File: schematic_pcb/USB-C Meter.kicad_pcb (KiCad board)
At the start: 2 copper layers, 49.4 x 45 mm, 57 parts, among them J1 USB_B_Micro, J2 USB-C Receptacle 6P, J3 Generic IN, J4 Generic OUT, J5 USB-C Receptacle 6P, J6 Conn_Coaxial, J7 UART, U1 XL1509-3.3, U2 ME6211C33, U3 TPS2115, U4 ESP32-C3FH4, U6 INA228, U7 Display I2C, Y1 40MHz

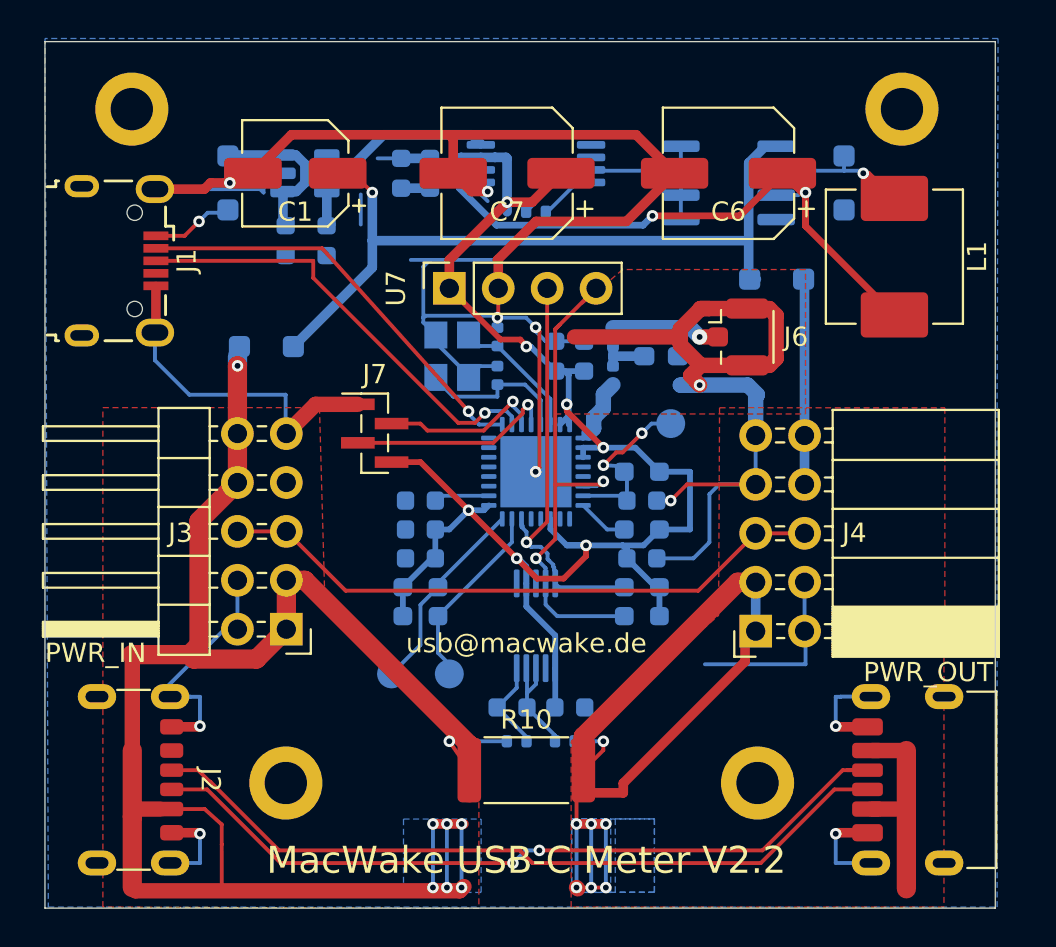
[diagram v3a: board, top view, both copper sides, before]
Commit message: feat(hw): new buck converter enables up to 48V PD input
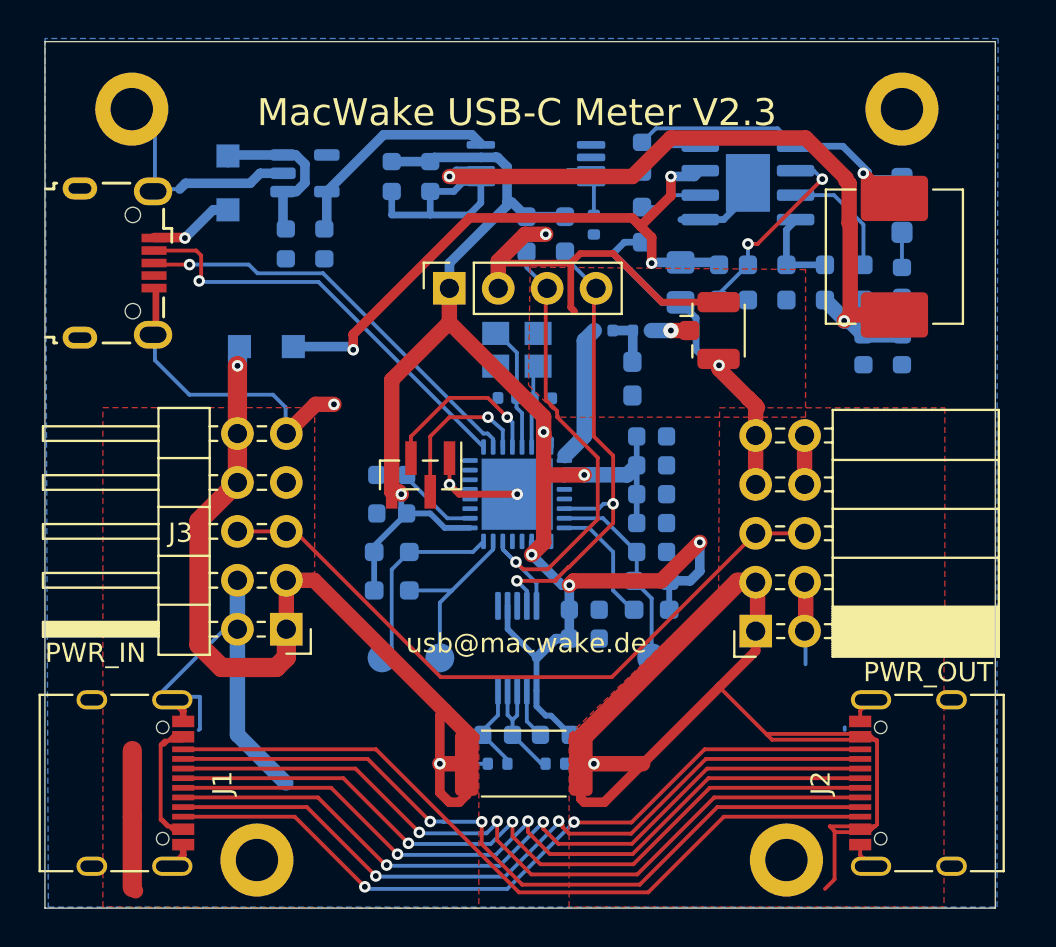
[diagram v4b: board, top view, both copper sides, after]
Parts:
- removed C2, C3: 10µF/10V, Capacitor_SMD:C_0603_1608Metric
- removed D4: 1N5819WS, Diode_SMD:D_SOD-123F
- removed U7: Display I2C, Connector_PinSocket_2.54mm:PinSocket_1x04_P2.54mm_Vertical
- added C19: 1µ, Capacitor_SMD:C_0603_1608Metric, B.Cu at (90.0, 47.7)
- added C22: 27pF, Capacitor_SMD:C_0402_1005Metric, B.Cu at (84.3, 44.2)
- added C23: 27pF, Capacitor_SMD:C_0402_1005Metric, B.Cu at (82.5, 44.2)
- added C24: 1pF, Capacitor_SMD:C_0402_1005Metric, B.Cu at (87.5, 40.7)
- added C25: 1pF, Capacitor_SMD:C_0402_1005Metric, B.Cu at (89.5, 40.7)
- added C26: 0.1µ, Capacitor_SMD:C_0603_1608Metric, B.Cu at (85.0, 61.7)
- added J8: UART, Connector_PinHeader_1.00mm:PinHeader_1x04_P1.00mm_Vertical_SMD_Pin1Left, F.Cu at (78.0, 48.2)
- added R15: 12k, Resistor_SMD:R_0603_1608Metric_Pad0.98x0.95mm_HandSolder, B.Cu at (76.5, 52.2)
- added R16: 12k, Resistor_SMD:R_0603_1608Metric_Pad0.98x0.95mm_HandSolder, B.Cu at (90.0, 53.7)
- added R5: 33k, Resistor_SMD:R_0603_1608Metric_Pad0.98x0.95mm_HandSolder, B.Cu at (95.0, 38.2)
- added R6: 200k, Resistor_SMD:R_0603_1608Metric_Pad0.98x0.95mm_HandSolder, B.Cu at (89.5, 35.2)
- added R7: 68k, Resistor_SMD:R_0603_1608Metric_Pad0.98x0.95mm_HandSolder, B.Cu at (99.0, 38.2)
- added R8: 22k, Resistor_SMD:R_0603_1608Metric_Pad0.98x0.95mm_HandSolder, B.Cu at (97.0, 38.2)
- C1: value 33µF/35V -> 0.1µ; footprint Capacitor_SMD:CP_Elec_5x5.8 -> Capacitor_SMD:C_0603_1608Metric; moved to B.Cu
- C10, C12: value 0.1µ -> 10µ
- C11: value 1µ -> 10µ
- C13: value 0.1µ -> 10µF
- C15: value 10n -> 0.1µ
- C17, C18: value 1pF -> 0.1µ; footprint Capacitor_SMD:C_0402_1005Metric -> Capacitor_SMD:C_0603_1608Metric
- C20: value 0.1µ -> 10n
- C21: value 0.1µF/6.3V -> 0.1µ
- C4: value 27pF -> 4.7µ; footprint Capacitor_SMD:C_0402_1005Metric -> Capacitor_SMD:C_0805_2012Metric_Pad1.18x1.45mm_HandSolder
- C5: value 27pF -> 10µ; footprint Capacitor_SMD:C_0402_1005Metric -> Capacitor_SMD:C_0603_1608Metric
- C6: value 220µF -> 10µ; footprint Capacitor_SMD:CP_Elec_6.3x5.9 -> Capacitor_SMD:C_0603_1608Metric; moved to B.Cu
- C7: value 220µF -> 0.1µ; footprint Capacitor_SMD:CP_Elec_6.3x5.9 -> Capacitor_SMD:C_0603_1608Metric; moved to B.Cu
- C8: value 0.1µ -> 2.2n
- C9: value 10µF -> 10µF/10V
- D1, D3: value 1N5819WS -> CMMSH1-60G; footprint Diode_SMD:D_SOD-123F -> Diode_SMD:Nexperia_CFP3_SOD-123W
- J1: value USB_B_Micro -> USB-C Receptacle 6P; footprint Connector_USB:USB_Micro-B_Wuerth_629105150521 -> Connector_USB:USB_C_Receptacle_XKB_U262-16XN-4BVC11
- J2: footprint Connector_USB:USB_C_Receptacle_GCT_USB4125-xx-x_6P_TopMnt_Horizontal -> Connector_USB:USB_C_Receptacle_XKB_U262-16XN-4BVC11
- J5: value USB-C Receptacle 6P -> USB_B_Micro; footprint Connector_USB:USB_C_Receptacle_HRO_TYPE-C-31-M-17 -> Connector_USB:USB_Micro-B_Wuerth_629105150521
- J6: value Conn_Coaxial -> Display I2C; footprint Connector_Coaxial:U.FL_Hirose_U.FL-R-SMT-1_Vertical -> Connector_PinSocket_2.54mm:PinSocket_1x04_P2.54mm_Vertical
- J7: value UART -> Conn_Coaxial; footprint Connector_PinHeader_1.00mm:PinHeader_1x04_P1.00mm_Vertical_SMD_Pin1Left -> Connector_Coaxial:U.FL_Hirose_U.FL-R-SMT-1_Vertical
- R1: value 3k3 -> 0.01R 3W; footprint Resistor_SMD:R_0603_1608Metric_Pad0.98x0.95mm_HandSolder -> Resistor_SMD:R_2512_6332Metric; moved to F.Cu
- R10: value 0.01R 3W -> 400R; footprint Resistor_SMD:R_2512_6332Metric -> Resistor_SMD:R_0402_1005Metric; moved to B.Cu
- R11: value 10R -> 3k3; footprint Resistor_SMD:R_0402_1005Metric -> Resistor_SMD:R_0603_1608Metric_Pad0.98x0.95mm_HandSolder
- R12: value 12k -> 3k3
- R2: value 3k3 -> 10R; footprint Resistor_SMD:R_0603_1608Metric_Pad0.98x0.95mm_HandSolder -> Resistor_SMD:R_0402_1005Metric
- R3: value 400R -> 10R
- R4: value 12k -> 100k
- R9: value 10R -> 56k; footprint Resistor_SMD:R_0402_1005Metric -> Resistor_SMD:R_0603_1608Metric_Pad0.98x0.95mm_HandSolder
- TP2: value Expansion -> Exp
- U1: value XL1509-3.3 -> MP4560DN; footprint Package_SO:SOIC-8_3.9x4.9mm_P1.27mm -> Package_SO:SOIC-8-1EP_3.9x4.9mm_P1.27mm_EP2.29x3mm
- moved J5 50.0 mm to (62.3, 37.2), turned to -90 degrees
- moved J2 42.5 mm to (104.5, 64.2), turned to 90 degrees
- moved C1 31.0 mm to (82.0, 61.7), turned to 0 degrees
- moved R9 29.9 mm to (101.0, 38.2), turned to 90 degrees
- moved R3 28.7 mm to (85.0, 63.2), turned to 0 degrees
- moved R10 28.5 mm to (87.0, 35.2), turned to -90 degrees
- moved J1 27.1 mm to (62.0, 64.2)
- moved C8 26.6 mm to (103.0, 38.2)
- moved R11 26.3 mm to (85.5, 35.7), turned to 90 degrees
- moved C10 23.2 mm to (73.0, 36.2), turned to -90 degrees
- moved C11 19.8 mm to (78.5, 32.7), turned to -90 degrees
- moved C5 19.0 mm to (101.0, 41.7)
- moved C12 18.4 mm to (76.5, 32.7), turned to -90 degrees
- moved J7 18.2 mm to (93.0, 40.7)
- moved R12 16.5 mm to (83.5, 35.7), turned to 90 degrees
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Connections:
- C1 pad 1: /VBUS_PD_R -> /SHNT+
- C1 pad 2: GND -> Net-(U6-Vbus)
- C10 pad 1: GND -> /VBUS_DATA_3V3
- C10 pad 2: 3V3 -> GND
- C12 pad 1: GND -> 3V3
- C12 pad 2: 3V3 -> GND
- C13 pad 1: GND -> 3V3
- C13 pad 2: Net-(U4-VDD_SPI) -> GND
- C14 pad 1: GND -> 3V3
- C14 pad 2: 3V3 -> GND
- C15 pad 1: GND -> 3V3
- C15 pad 2: 3V3 -> GND
- C16 pad 2: Net-(U4-CHIP_EN) -> 3V3
- C17 pad 1: /RF -> GND
- C17 pad 2: Net-(C17-Pad2) -> 3V3
- C18 pad 1: /ANT -> GND
- C18 pad 2: Net-(C17-Pad2) -> Net-(U4-VDD_SPI)
- C20 pad 1: 3V3 -> GND
- C20 pad 2: GND -> 3V3
- C21 pad 1: /SHNT+ -> GND
- C21 pad 2: /SHNT- -> Net-(U4-CHIP_EN)
- C4 pad 1: Net-(U4-XTAL_N) -> /VBUS_PD_R
- C5 pad 1: GND -> /VBUS_PD_3V3
- C5 pad 2: Net-(U4-XTAL_P) -> GND
- C7 pad 1: 3V3 -> Net-(U1-BST)
- C7 pad 2: GND -> Net-(D2-K)
- C8 pad 1: 3V3 -> Net-(C8-Pad1)
- C9 pad 1: 3V3 -> /VBUS_DATA_R
- J2 pad A9: /VBUS_PD_1_IN -> /VBUS_PD_2_IN
- J2 pad B9: /VBUS_PD_1_IN -> /VBUS_PD_2_IN
- J6 pad 1: /ANT -> 3V3
- J7 pad 1: GND -> /ANT
- J7 pad 2: Net-(J7-Pin_2) -> GND
- L2 pad 2: Net-(C17-Pad2) -> Net-(C24-Pad2)
- R1 pad 1: SDA -> /VBUS_PD_1_IN
- R1 pad 2: 3V3 -> /VBUS_PD_2_IN
- R10 pad 1: /VBUS_PD_1_IN -> Net-(U3-ILIM)
- R10 pad 2: /VBUS_PD_2_IN -> GND
- R11 pad 1: /SHNT- -> SDA
- R11 pad 2: /VBUS_PD_2_IN -> 3V3
- R12 pad 1: Net-(U4-GPIO3) -> SCL
- R13 pad 1: Net-(U4-GPIO9) -> Net-(U4-GPIO3)
- R14 pad 1: Net-(U4-GPIO10) -> Net-(U4-GPIO9)
- R2 pad 1: SCL -> /VBUS_PD_1_IN
- R2 pad 2: 3V3 -> /SHNT+
- R3 pad 1: Net-(U3-ILIM) -> Net-(U6-Vbus)
- R3 pad 2: GND -> /VBUS_PD_2_IN
- R4 pad 1: Net-(U4-CHIP_EN) -> Net-(U1-EN)
- R4 pad 2: 3V3 -> /VBUS_PD_R
- R9 pad 1: /SHNT+ -> Net-(C8-Pad1)
- R9 pad 2: /VBUS_PD_1_IN -> Net-(U1-COMP)
- U1 pad 1: /VBUS_PD_R -> Net-(D2-K)
- U1 pad 2: Net-(D2-K) -> Net-(U1-EN)
- U1 pad 3: /VBUS_PD_3V3 -> Net-(U1-COMP)
- U1 pad 4: GND -> Net-(U1-FB)
- U1 pad 6: GND -> Net-(U1-FREQ)
- U1 pad 7: GND -> /VBUS_PD_R
- U1 pad 8: GND -> Net-(U1-BST)
- U4 pad 25: Net-(J1-D-) -> /D-
- U4 pad 26: Net-(J1-D+) -> /D+
- U4 pad 27: Net-(J7-Pin_2) -> Net-(J8-Pin_2)
- U4 pad 28: Net-(J7-Pin_3) -> Net-(J8-Pin_3)
- U6 pad 8: /SHNT- -> Net-(U6-Vbus)
- U6 pad 9: /SHNT- -> Net-(U6-Vbus)
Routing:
- net GND: track 206.0 -> 126.4 mm, vias 11 -> 5
- net /VBUS_PD_1_IN: track 111.5 -> 66.2 mm, vias 8 -> 2
- net Net-(J1-D--PadB7): track 0.00 -> 40.2 mm, vias 0 -> 2
- net Net-(J1-D+-PadA6): track 0.00 -> 40.1 mm, vias 0 -> 2
- net Net-(J1-D--PadA7): track 0.00 -> 40.1 mm, vias 0 -> 2
- net Net-(J1-D+-PadB6): track 0.00 -> 39.9 mm, vias 0 -> 2
- net Net-(J1-SBU2): track 0.00 -> 39.9 mm
- net Net-(J1-SBU1): track 0.00 -> 39.8 mm, vias 0 -> 2
- net Net-(J1-D+): track 23.3 -> 0.00 mm, vias 1 -> 0
- net /D-: track 0.00 -> 22.3 mm, vias 0 -> 1
- net Net-(J1-D-): track 22.1 -> 0.00 mm, vias 1 -> 0
- net /D+: track 0.00 -> 21.7 mm, vias 0 -> 1
- net Net-(J7-Pin_3): track 11.1 -> 0.00 mm, vias 1 -> 0
- net 3V3: track 86.6 -> 97.0 mm, vias 7 -> 6
- net Net-(D2-K): track 7.50 -> 17.6 mm
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- removed copper zone on B.Cu, net /VBUS_PD_1_IN
- removed copper zone on B.Cu, net /VBUS_PD_2_IN
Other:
- board text added: "MacWake USB-C Meter V2.3"
- board text removed: "MacWake USB-C Meter V2.0"
- board text removed: "MacWake USB-C Meter V2.2"

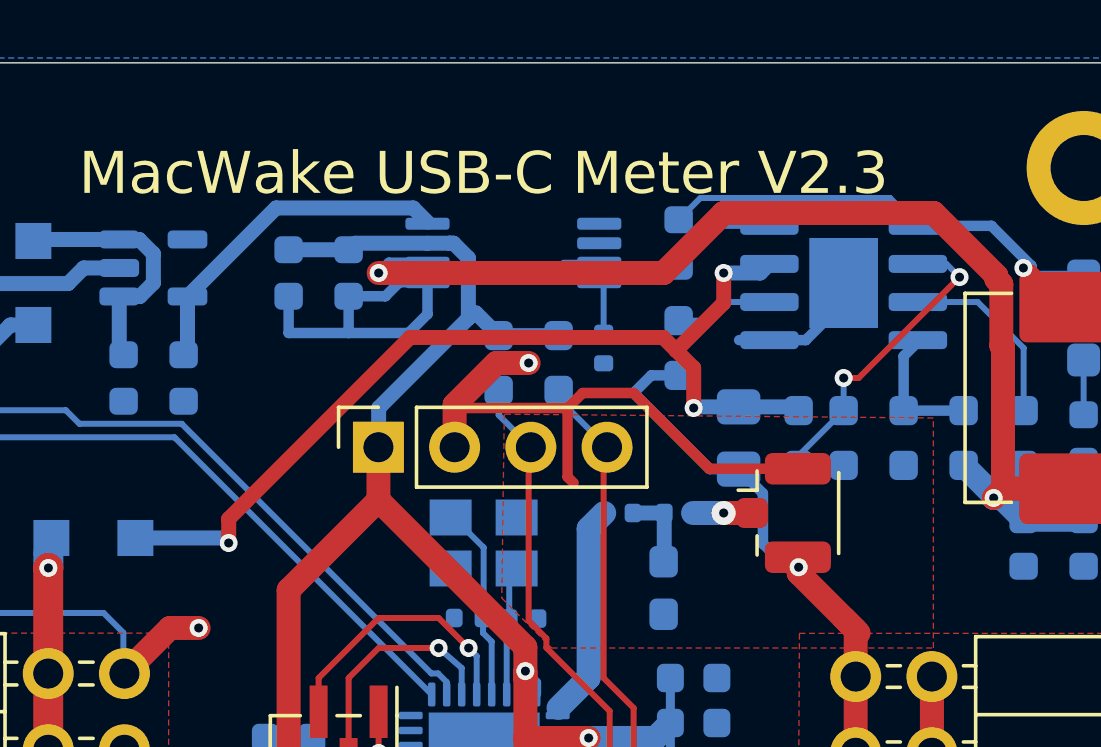
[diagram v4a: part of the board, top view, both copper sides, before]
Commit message: feat: schematic improvements (fix some component values)
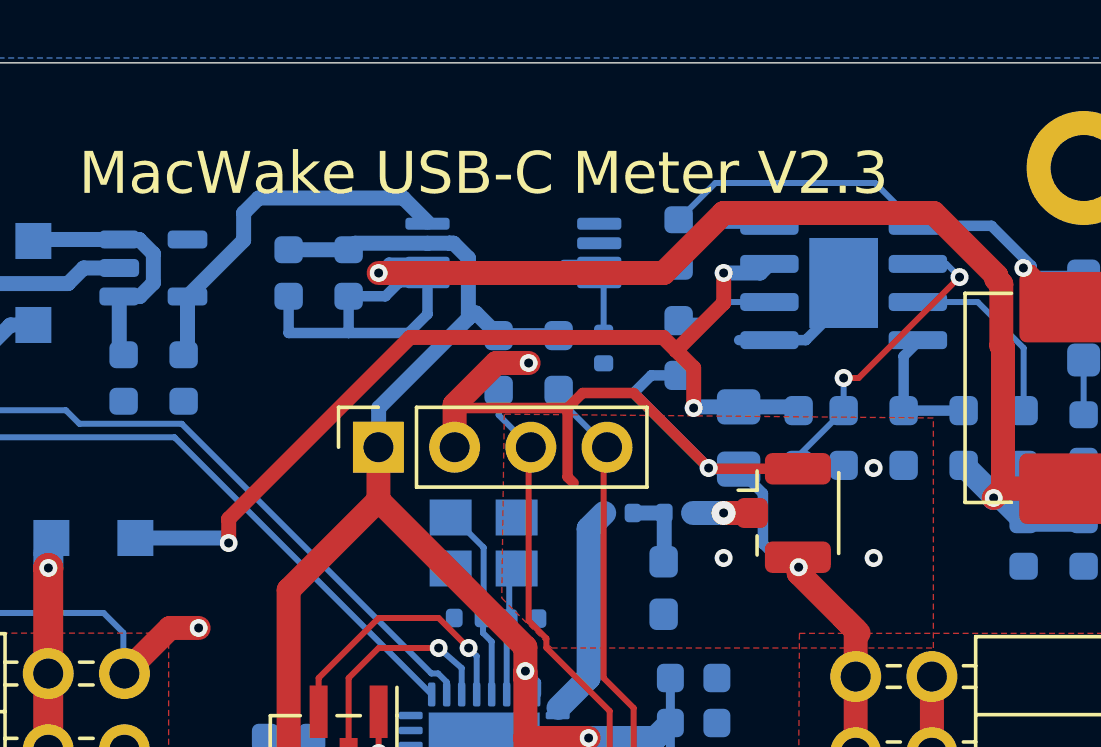
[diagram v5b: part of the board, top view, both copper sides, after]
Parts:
- C11, C12: value 10µ -> 22µ
- C13: value 10µF -> 10µ
- C22, C23: value 27pF -> 15pF
- C9: value 10µF/10V -> 10µ
- J1, J2: value USB-C Receptacle 6P -> USB-C 12P
- J6: value Display I2C -> Display
- J7: value Conn_Coaxial -> U.FL
- L2: value 2.7nH -> 3.9nH
- R10: value 400R -> 400
- R5: value 33k -> 56k
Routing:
- net /VBUS_DATA_3V3: track 11.2 -> 12.0 mm
- net GND: vias 5 -> 9

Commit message: fix: schematic/pcb v2.4 (wip)
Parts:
- removed MH1, MH2: MountingHole_2.2mm_M2_DIN965_Pad, MountingHole:MountingHole_2.2mm_M2_DIN965_Pad
- added ?: , , F.Cu at (106.0, 29.0)
- added ?: , , F.Cu at (62.5, 29.0)
- added MH3: MountingHole_3.2mm_M3_Pad_TopBottom, MountingHole:MountingHole_3.2mm_M3_Pad_TopBottom, F.Cu at (106.0, 29.0)
- added MH3: MountingHole_3.2mm_M3_Pad_TopBottom, MountingHole:MountingHole_3.2mm_M3_Pad_TopBottom, F.Cu at (62.5, 29.0)
- MH3, MH4: value MountingHole_2.2mm_M2_DIN965_Pad -> MountingHole_3.2mm_M3_Pad_TopBottom; footprint MountingHole:MountingHole_2.2mm_M2_DIN965_Pad -> MountingHole:MountingHole_3.2mm_M3_Pad_TopBottom
- moved R1 5.17 mm to (83.4, 58.0)
- moved MH4 3.30 mm to (99.5, 66.0)
- moved J4 3.14 mm to (98.3, 55.1)
- moved J2 2.98 mm to (107.2, 63.0)
- moved MH3 2.23 mm to (69.0, 66.0)
- moved J3 1.43 mm to (70.2, 55.0)
- moved J1 1.39 mm to (61.2, 63.0)
- moved J6 1.00 mm to (79.5, 37.5)
- moved J7 0.50 mm to (93.0, 40.2)
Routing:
- net /VBUS_PD_2_IN: track 69.6 -> 26.4 mm
- net Net-(J1-D--PadB7): track 40.2 -> 0.00 mm, vias 2 -> 0
- net /CC1: track 40.2 -> 0.00 mm, vias 2 -> 0
- net Net-(J1-D+-PadA6): track 40.1 -> 0.00 mm, vias 2 -> 0
- net Net-(J1-D--PadA7): track 40.1 -> 0.00 mm, vias 2 -> 0
- net Net-(J1-D+-PadB6): track 39.9 -> 0.00 mm, vias 2 -> 0
- net Net-(J1-SBU2): track 39.9 -> 0.00 mm
- net Net-(J1-SBU1): track 39.8 -> 0.00 mm, vias 2 -> 0
- net /CC2: track 39.7 -> 0.00 mm, vias 2 -> 0
- net /VBUS_PD_1_IN: track 66.2 -> 45.4 mm
- net GND: track 126.4 -> 110.3 mm
- net /CHGR_ID_GENERIC: track 35.2 -> 33.7 mm
- added copper zone on In1.Cu, net GND
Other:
- board size 49.4 x 45 mm -> 51.5 x 45 mm
- copper layers 2 -> 4
- board text added: "MacWake USB-C Meter V2.4"
- board text removed: "MacWake USB-C Meter V2.3"
